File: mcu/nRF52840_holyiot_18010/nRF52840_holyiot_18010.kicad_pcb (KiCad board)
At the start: 2 copper layers, 3 parts

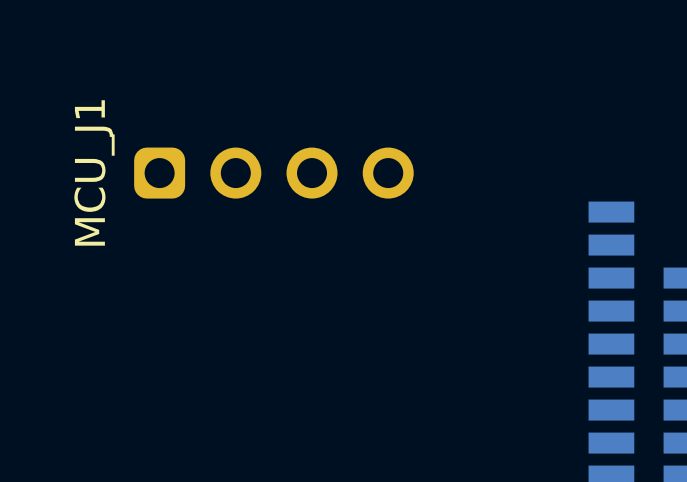
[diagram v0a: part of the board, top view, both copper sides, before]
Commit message: correct mcu side
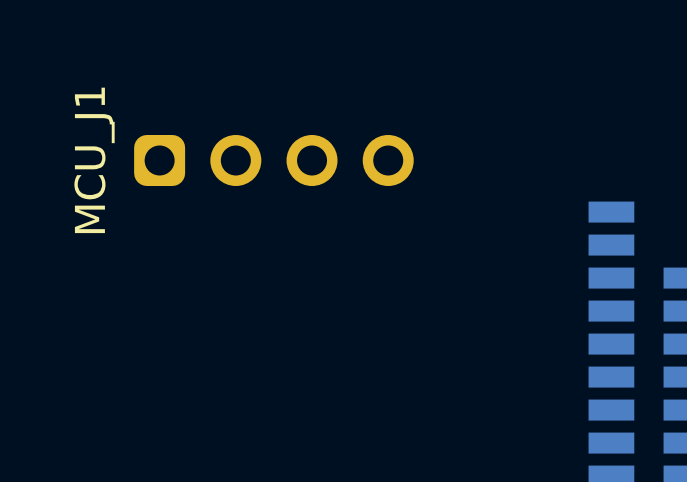
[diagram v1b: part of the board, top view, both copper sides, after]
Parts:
- moved MCU_J1 0.42 mm to (-18.0, -6.70)
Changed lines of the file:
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@@
 	(footprint "ErgoCai.pretty:Connector_THT_1x4_2.54"
 		(layer "F.Cu")
-		(at -18 -6.281 90)
+		(at -18 -6.7 90)
 		(property "Reference" "MCU_J1"
 			(at 0 -6.096 90)

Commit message: update battery module
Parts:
- moved MCU_SW1 3.01 mm to (20.0, 2.50)
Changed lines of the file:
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@@
 	(footprint "ErgoCai.pretty:K2-1187SQ"
 		(layer "B.Cu")
-		(at 17 2.719)
+		(at 20 2.5)
 		(property "Reference" "MCU_SW1"
 			(at 0 3.683 180)

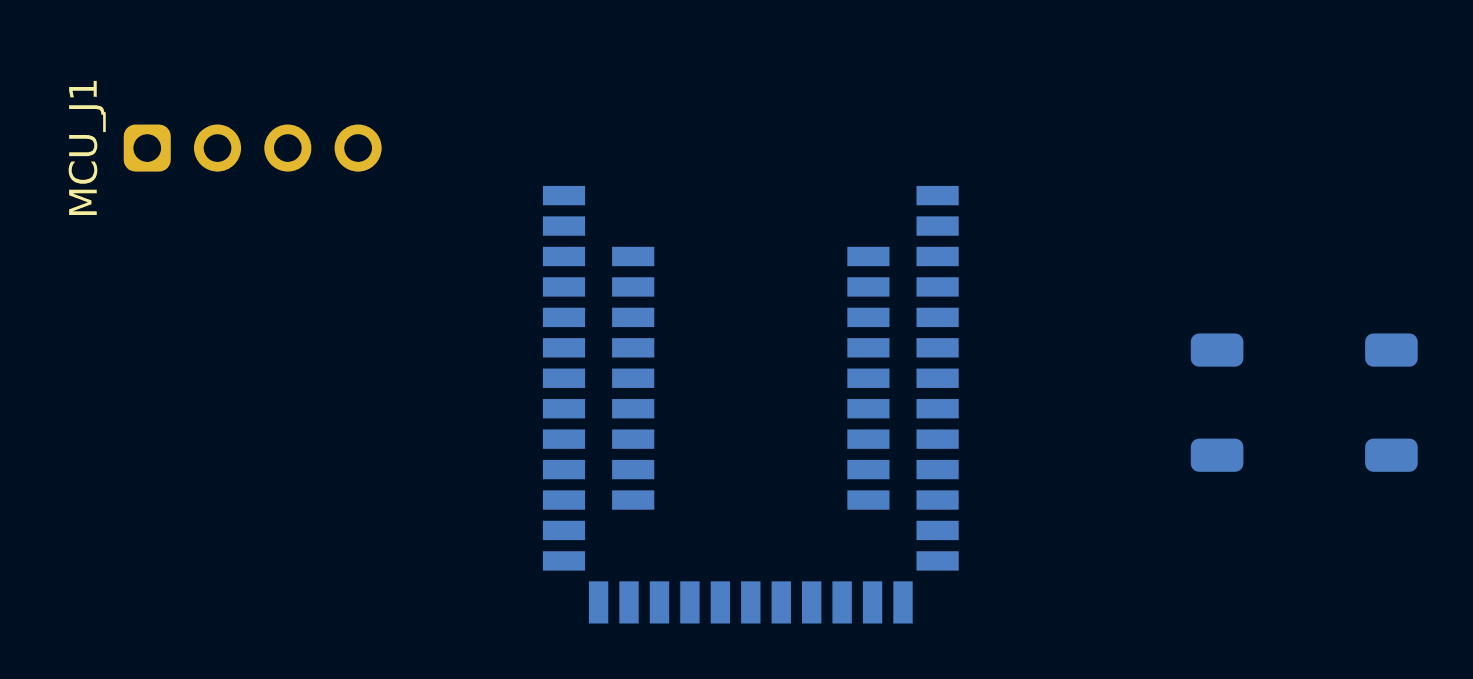
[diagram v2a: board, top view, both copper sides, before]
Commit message: add track between gnd in mcu
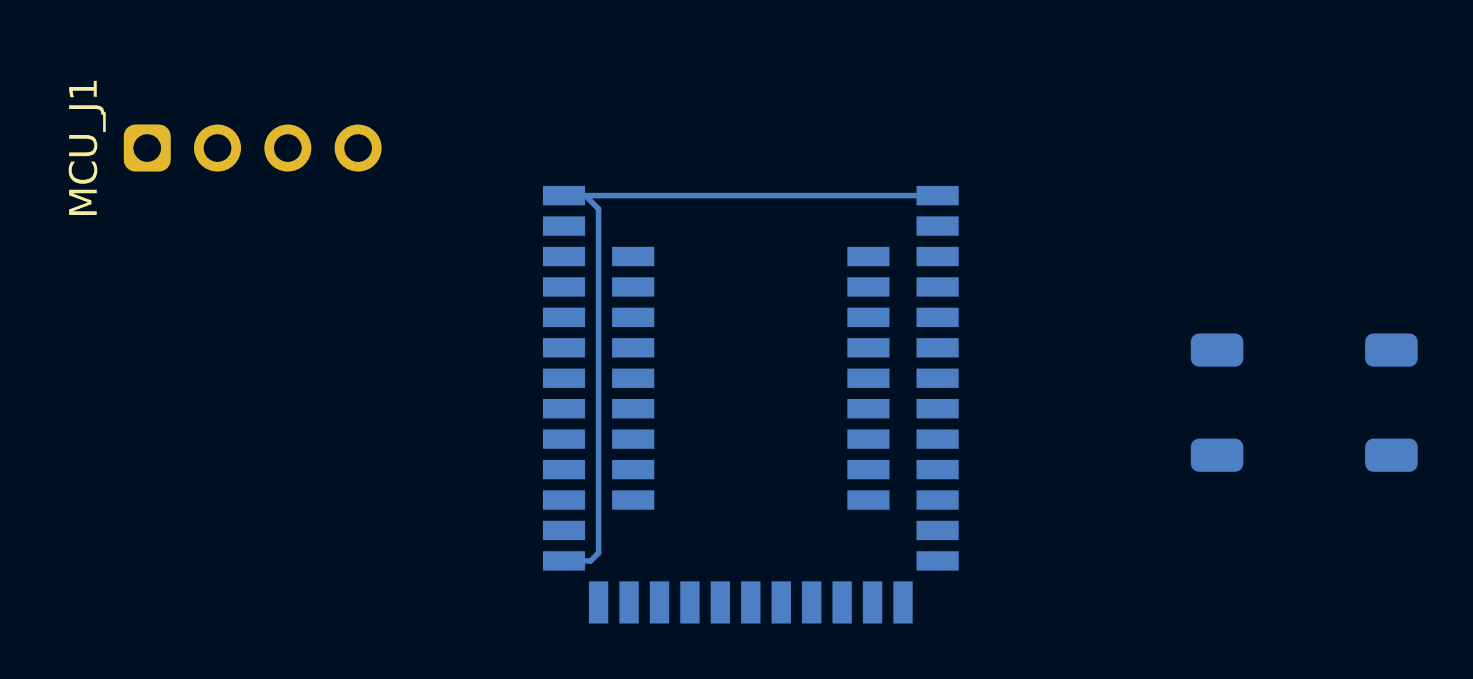
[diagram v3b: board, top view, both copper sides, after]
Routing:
- net GND: track 0.00 -> 28.7 mm
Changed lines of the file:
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@@
 		)
+	)
+	(segment
+		(start -5.788 8.219)
+		(end -5.5 7.931)
+		(width 0.2)
+		(layer "B.Cu")
+		(net 3)
+	)
+	(segment
+		(start -5.5 7.931)
+		(end -5.5 -4.5)
+		(width 0.2)
+		(layer "B.Cu")
+		(net 3)
+	)
+	(segment
+		(start -5.5 -4.5)
+		(end -5.981 -4.981)
+		(width 0.2)
+		(layer "B.Cu")
+		(net 3)
+	)
+	(segment
+		(start -6.75 8.219)
+		(end -5.788 8.219)
+		(width 0.2)
+		(layer "B.Cu")
+		(net 3)
+	)
+	(segment
+		(start -6.75 -4.981)
+		(end 6.75 -4.981)
+		(width 0.2)
+		(layer "B.Cu")
+		(net 3)
+	)
+	(segment
+		(start -5.981 -4.981)
+		(end -6.75 -4.981)
+		(width 0.2)
+		(layer "B.Cu")
+		(net 3)
 	)
 	(embedded_fonts no)

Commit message: move mcu to (0, 0)
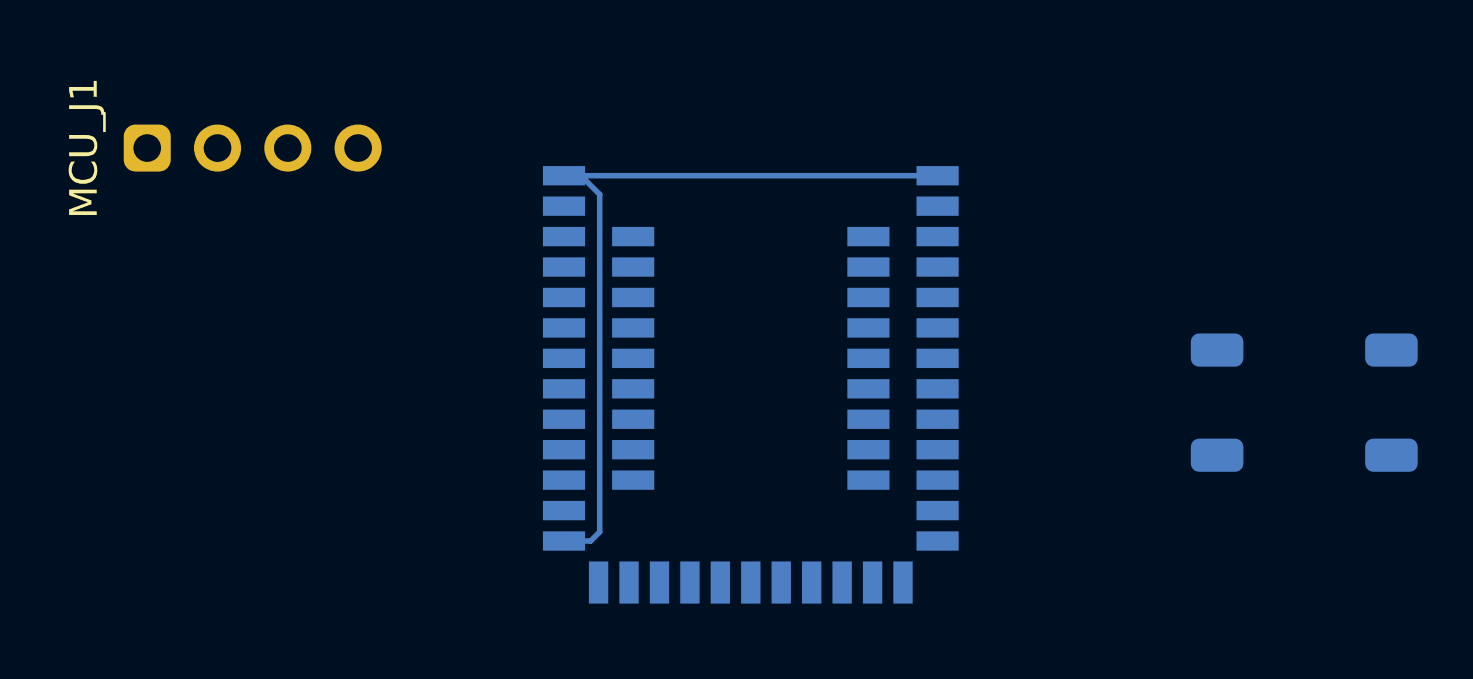
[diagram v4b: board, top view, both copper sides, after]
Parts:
- moved MCU_U1 0.72 mm to (0.00, 0.00)
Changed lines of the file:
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@@
 	(footprint "ErgoCai.pretty:nRF52840_holyiot_18010"
 		(layer "B.Cu")
-		(at 0 0.719 180)
+		(at 0 0 180)
 		(descr "Module containing a nRF52840 and most passives and antenna")
 		(tags "holyiot 18010 nRF52840 bluetooth low energy ")
@@
 			(polygon
 				(pts
-					(xy 9.5 -5.481) (xy 9.5 -10.481) (xy -9.5 -10.481) (xy -9.5 -5.481)
+					(xy 9.5 -6.2) (xy 9.5 -11.2) (xy -9.5 -11.2) (xy -9.5 -6.2)
 				)
 			)
@@
 	)
 	(segment
-		(start -5.788 8.219)
-		(end -5.5 7.931)
+		(start -6.75 -5.7)
+		(end 6.75 -5.7)
 		(width 0.2)
 		(layer "B.Cu")
@@
 	)
 	(segment
-		(start -5.5 7.931)
-		(end -5.5 -4.5)
+		(start -5.46 7.172)
+		(end -5.46 -5.024)
 		(width 0.2)
 		(layer "B.Cu")
@@
 	)
 	(segment
-		(start -5.5 -4.5)
-		(end -5.981 -4.981)
+		(start -5.46 -5.024)
+		(end -6.136 -5.7)
 		(width 0.2)
 		(layer "B.Cu")
@@
 	)
 	(segment
-		(start -6.75 8.219)
-		(end -5.788 8.219)
+		(start -6.136 -5.7)
+		(end -6.75 -5.7)
 		(width 0.2)
 		(layer "B.Cu")
@@
 	)
 	(segment
-		(start -6.75 -4.981)
-		(end 6.75 -4.981)
+		(start -6.75 7.5)
+		(end -5.788 7.5)
 		(width 0.2)
 		(layer "B.Cu")
@@
 	)
 	(segment
-		(start -5.981 -4.981)
-		(end -6.75 -4.981)
+		(start -5.788 7.5)
+		(end -5.46 7.172)
 		(width 0.2)
 		(layer "B.Cu")

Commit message: use nrf52840 simple
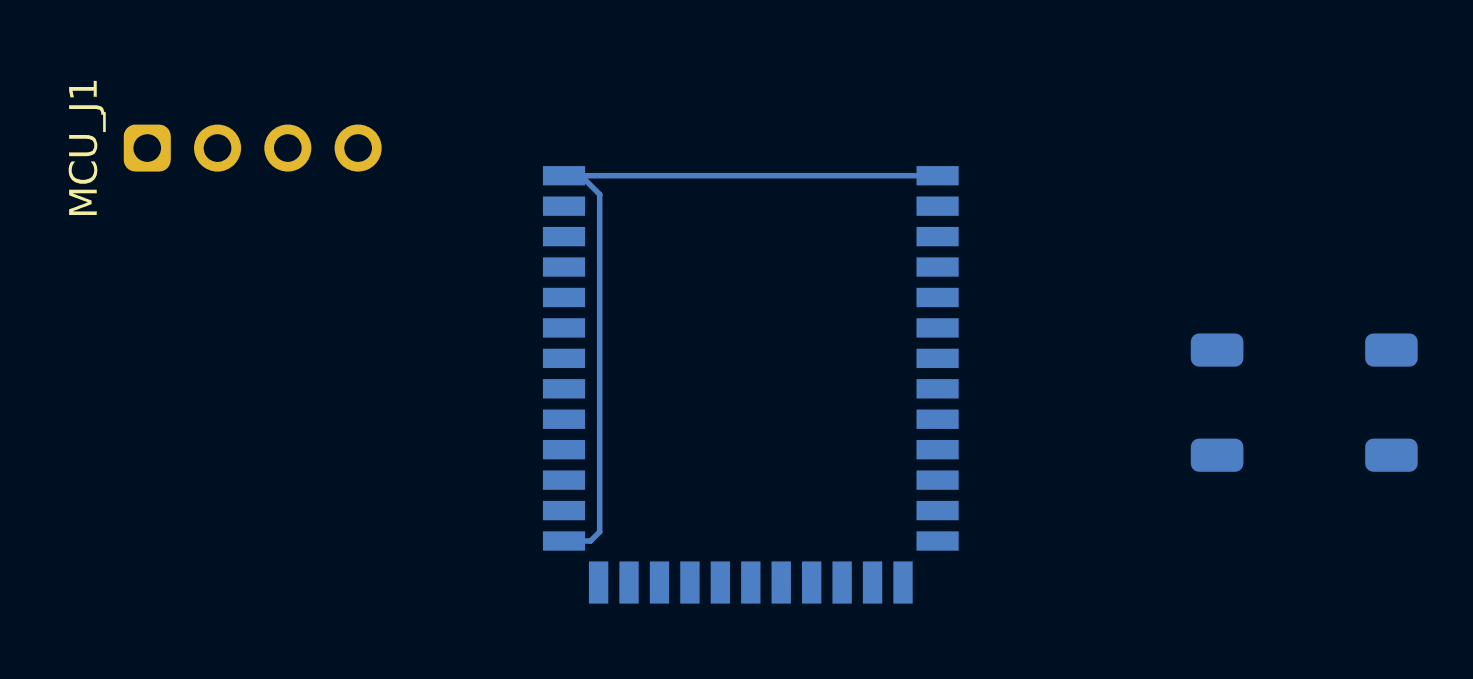
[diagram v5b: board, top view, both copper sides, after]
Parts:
- MCU_U1: value nRF52840_holyiot_18010 -> nRF52840_holyiot_18010_Simple; footprint ErgoCai.pretty:nRF52840_holyiot_18010 -> ErgoCai.pretty:nRF52840_holyiot_18010_HS_simple
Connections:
- MCU_U1 pad 10: unconnected-(MCU_U1-P0.30-LF-A-Pad10) -> AnalogInput
- MCU_U1 pad 11: unconnected-(MCU_U1-P0.31-LF-A-Pad11) -> AnalogInput
- MCU_U1 pad 12: unconnected-(MCU_U1-P0.04-A-Pad12) -> AnalogInput
- MCU_U1 pad 13: unconnected-(MCU_U1-P0.05-A-Pad13) -> AnalogInput
- MCU_U1 pad 37: GND -> unconnected-(MCU_U1-GND-Pad37)
- MCU_U1 pad 6: unconnected-(MCU_U1-P0.03-LF-A-Pad6) -> AnalogInput
- MCU_U1 pad 7: unconnected-(MCU_U1-P0.02-LF-A-Pad7) -> AnalogInput
- MCU_U1 pad 8: unconnected-(MCU_U1-P0.28-LF-A-Pad8) -> AnalogInput
- MCU_U1 pad 9: unconnected-(MCU_U1-P0.29-LF-A-Pad9) -> AnalogInput

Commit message: replace VDD-nRF to VCC
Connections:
- net nRF_VDD renamed VCC
- MCU_U1 pad 10: AnalogInput -> ADC_5
- MCU_U1 pad 11: AnalogInput -> ADC_6
- MCU_U1 pad 12: AnalogInput -> ADC_7
- MCU_U1 pad 13: AnalogInput -> ADC_8
- MCU_U1 pad 37: unconnected-(MCU_U1-GND-Pad37) -> GND
- MCU_U1 pad 6: AnalogInput -> ADC_1
- MCU_U1 pad 7: AnalogInput -> ADC_2
- MCU_U1 pad 8: AnalogInput -> ADC_3
- MCU_U1 pad 9: AnalogInput -> ADC_4
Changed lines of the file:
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@@
 	(net 0 "")
 	(net 1 "SWD")
-	(net 2 "nRF_VDD")
+	(net 2 "VCC")
 	(net 3 "GND")
 	(net 4 "SWC")
@@
 	(net 10 "unconnected-(MCU_U1-P0.19-Pad20)")
 	(net 11 "unconnected-(MCU_U1-P1.04-Pad33)")
-	(net 12 "unconnected-(MCU_U1-GND-Pad37)")
+	(net 12 "ADC_8")
 	(net 13 "unconnected-(MCU_U1-P0.23-Pad18)")
-	(net 14 "AnalogInput")
+	(net 14 "ADC_6")
 	(net 15 "unconnected-(MCU_U1-P0.09{slash}NFC1-Pad35)")
 	(net 16 "unconnected-(MCU_U1-P0.21-Pad19)")
@@
 	(net 28 "unconnected-(MCU_U1-P0.07-Pad15)")
 	(net 29 "VBUS")
+	(net 30 "ADC_4")
+	(net 31 "ADC_2")
+	(net 32 "ADC_1")
+	(net 33 "ADC_7")
+	(net 34 "ADC_3")
+	(net 35 "ADC_5")
 	(footprint "ErgoCai.pretty:Connector_THT_1x4_2.54"
 		(layer "F.Cu")
@@
 			(layers "*.Cu" "*.Mask")
 			(remove_unused_layers no)
-			(net 2 "nRF_VDD")
+			(net 2 "VCC")
 			(pinfunction "Pin_2")
 			(pintype "passive")
@@
 			(size 1.524 0.7)
 			(layers "B.Cu" "B.Mask" "B.Paste")
-			(net 14 "AnalogInput")
+			(net 32 "ADC_1")
 			(pinfunction "P0.03/AIN1")
 			(pintype "input")
@@
 			(size 1.524 0.7)
 			(layers "B.Cu" "B.Mask" "B.Paste")
-			(net 14 "AnalogInput")
+			(net 31 "ADC_2")
 			(pinfunction "P0.02/AIN0")
 			(pintype "input")
@@
 			(size 1.524 0.7)
 			(layers "B.Cu" "B.Mask" "B.Paste")
-			(net 14 "AnalogInput")
+			(net 34 "ADC_3")
 			(pinfunction "P0.28/AIN4")
 			(pintype "input")
@@
 			(size 1.524 0.7)
 			(layers "B.Cu" "B.Mask" "B.Paste")
-			(net 14 "AnalogInput")
+			(net 30 "ADC_4")
 			(pinfunction "P0.29/AIN5")
 			(pintype "input")
@@
 			(size 1.524 0.7)
 			(layers "B.Cu" "B.Mask" "B.Paste")
-			(net 14 "AnalogInput")
+			(net 35 "ADC_5")
 			(pinfunction "P0.30/AIN6")
 			(pintype "input")
@@
 			(size 1.524 0.7)
 			(layers "B.Cu" "B.Mask" "B.Paste")
-			(net 14 "AnalogInput")
+			(net 14 "ADC_6")
 			(pinfunction "P0.31/AIN7")
 			(pintype "input")
@@
 			(size 1.524 0.7)
 			(layers "B.Cu" "B.Mask" "B.Paste")
-			(net 14 "AnalogInput")
+			(net 33 "ADC_7")
 			(pinfunction "P0.04/AIN2")
 			(pintype "input")
@@
 			(size 1.524 0.7)
 			(layers "B.Cu" "B.Mask" "B.Paste")
-			(net 14 "AnalogInput")
+			(net 12 "ADC_8")
 			(pinfunction "P0.05/AIN3")
 			(pintype "input")
@@
 			(size 1.524 0.7)
 			(layers "B.Cu" "B.Mask" "B.Paste")
-			(net 2 "nRF_VDD")
+			(net 2 "VCC")
 			(pinfunction "VDD")
 			(pintype "power_in")
@@
 			(size 1.524 0.7)
 			(layers "B.Cu" "B.Mask" "B.Paste")
-			(net 12 "unconnected-(MCU_U1-GND-Pad37)")
+			(net 3 "GND")
 			(pinfunction "GND")
 			(pintype "power_in")

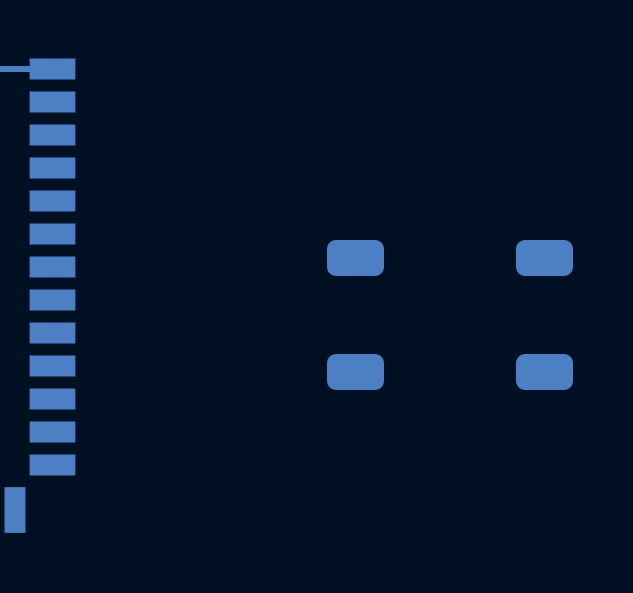
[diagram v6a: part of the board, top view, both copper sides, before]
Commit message: add connection between reset
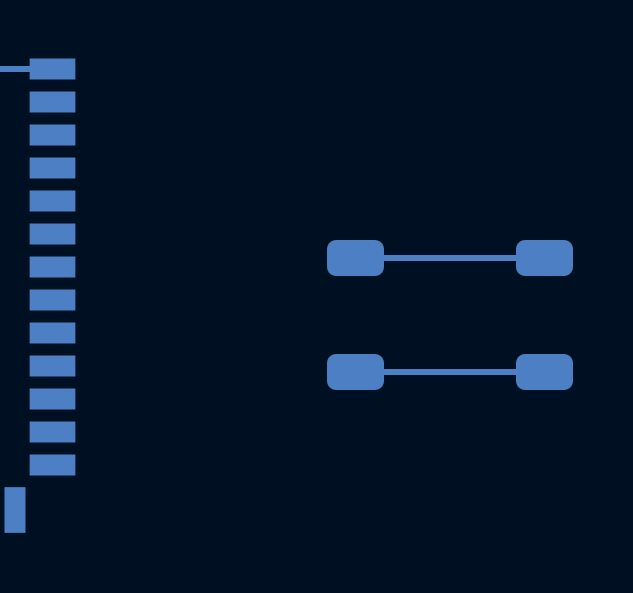
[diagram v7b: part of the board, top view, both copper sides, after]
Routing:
- net RESET: track 0.00 -> 6.30 mm
- net GND: track 28.7 -> 35.0 mm
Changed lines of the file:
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@@
+	)
+	(segment
+		(start 16.85 0.6)
+		(end 23.15 0.6)
+		(width 0.2)
+		(layer "B.Cu")
+		(net 3)
 	)
 	(segment
@@
 		(net 3)
 	)
+	(segment
+		(start 16.85 4.4)
+		(end 23.15 4.4)
+		(width 0.2)
+		(layer "B.Cu")
+		(net 5)
+	)
 	(embedded_fonts no)
